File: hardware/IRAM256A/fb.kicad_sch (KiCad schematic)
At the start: 48 parts

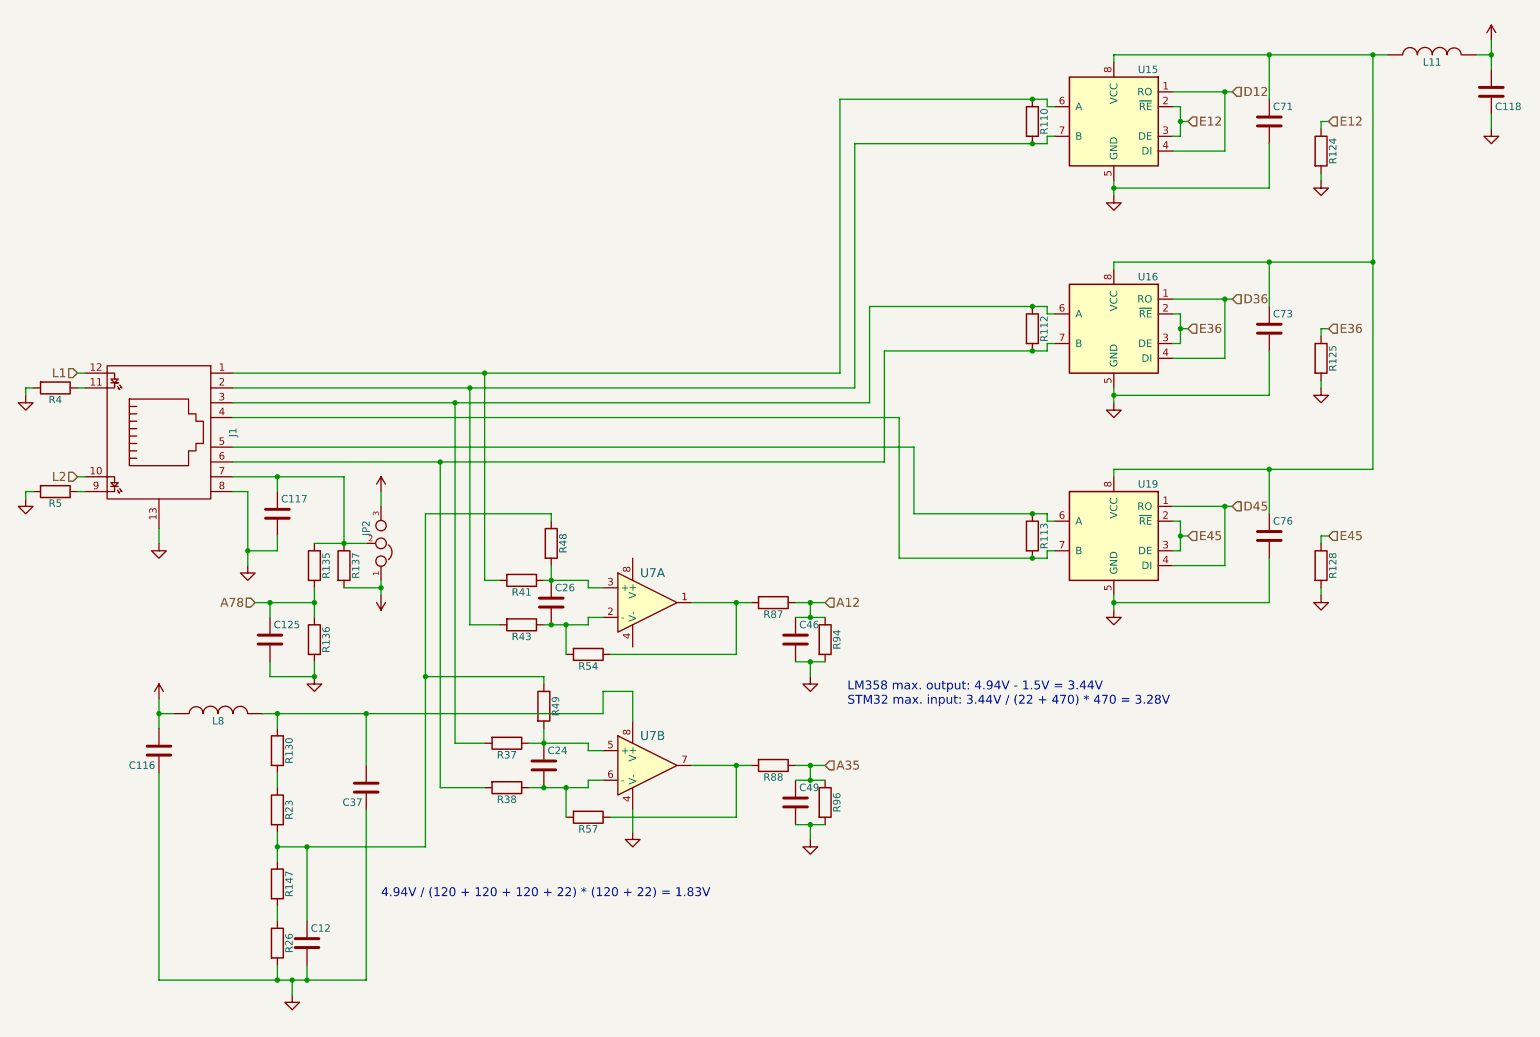
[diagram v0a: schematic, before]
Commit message: Structure change + kicad 3d models updated
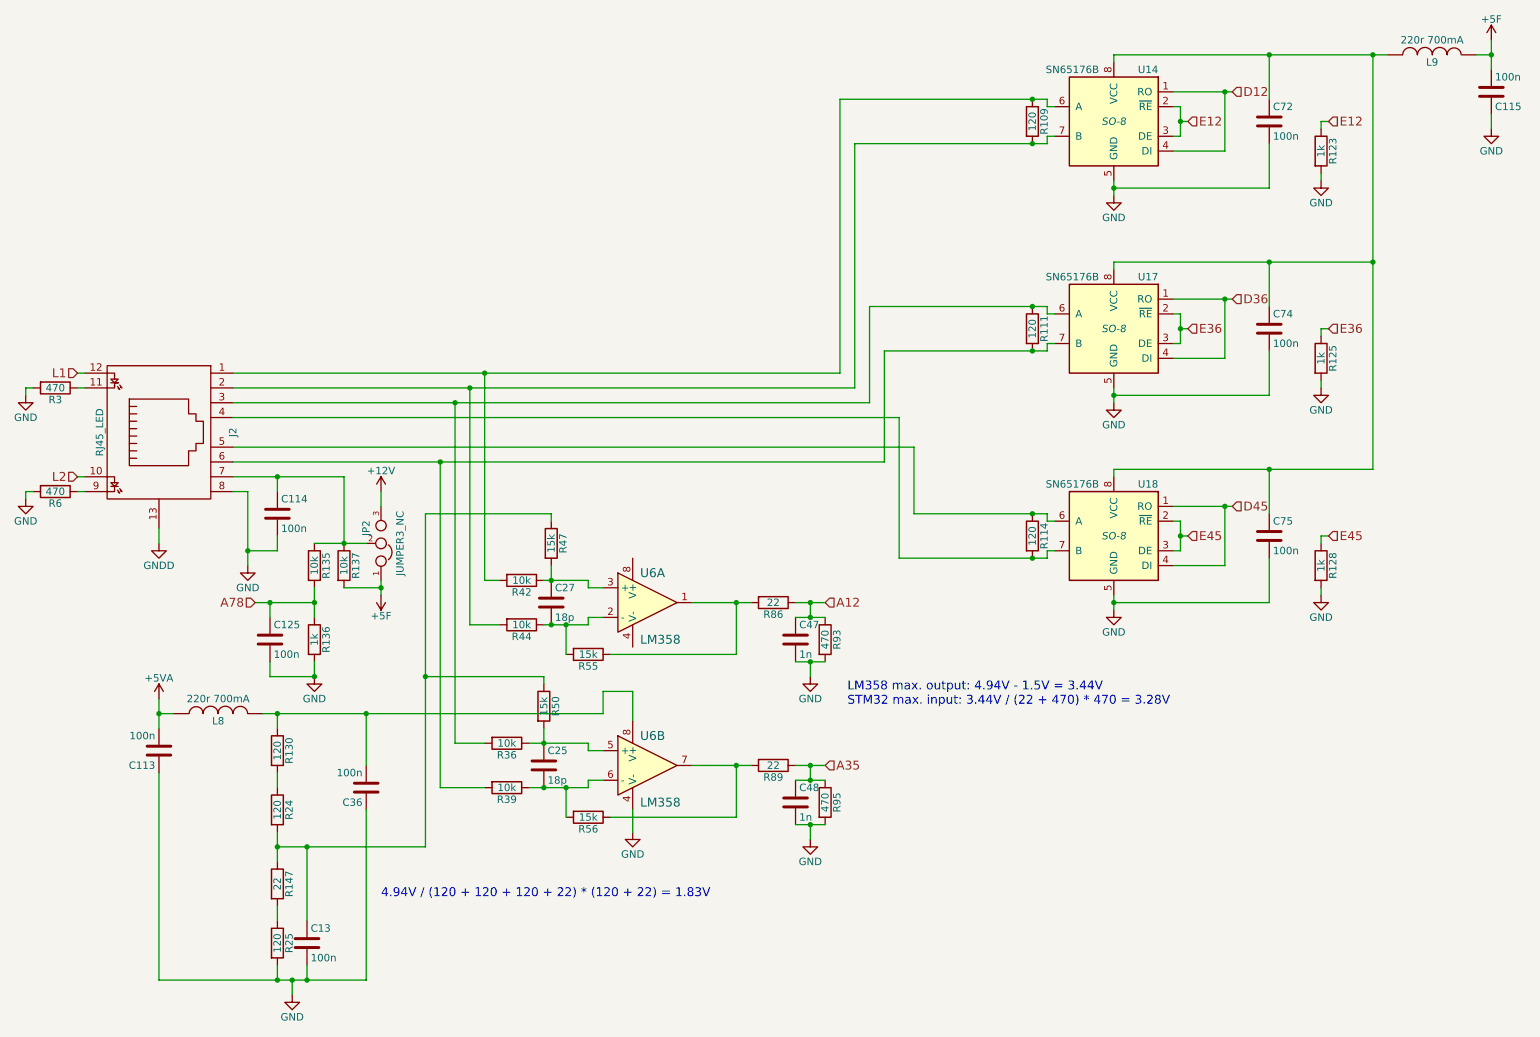
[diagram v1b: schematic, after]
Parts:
- C113: renamed from C116; value (none) -> 100n; footprint (none) -> stmbl:C_0603
- C114: renamed from C117; value (none) -> 100n; footprint (none) -> stmbl:C_0603
- C115: renamed from C118; value (none) -> 100n; footprint (none) -> stmbl:C_0603
- C125: value (none) -> 100n; footprint (none) -> stmbl:C_0603
- C13: renamed from C12; value (none) -> 100n; footprint (none) -> stmbl:C_0603
- C25: renamed from C24; value (none) -> 18p; footprint (none) -> stmbl:C_0603
- C27: renamed from C26; value (none) -> 18p; footprint (none) -> stmbl:C_0603
- C36: renamed from C37; value (none) -> 100n; footprint (none) -> stmbl:C_0603
- C47: renamed from C46; value (none) -> 1n; footprint (none) -> stmbl:C_0603
- C48: renamed from C49; value (none) -> 1n; footprint (none) -> stmbl:C_0603
- C72: renamed from C71; value (none) -> 100n; footprint (none) -> stmbl:C_0603
- C74: renamed from C73; value (none) -> 100n; footprint (none) -> stmbl:C_0603
- C75: renamed from C76; value (none) -> 100n; footprint (none) -> stmbl:C_0603
- J2: renamed from J1; value (none) -> RJ45_LED; footprint (none) -> stmbl:RJ45_LED
- JP2: value (none) -> JUMPER3_NC; footprint (none) -> stmbl:SOLDER_JUMPER_3_NC
- L8: value (none) -> 220r 700mA; footprint (none) -> stmbl:R_0603
- L9: renamed from L11; value (none) -> 220r 700mA; footprint (none) -> stmbl:R_0603
- R109: renamed from R110; value (none) -> 120; footprint (none) -> stmbl:R_0603
- R111: renamed from R112; value (none) -> 120; footprint (none) -> stmbl:R_0603
- R114: renamed from R113; value (none) -> 120; footprint (none) -> stmbl:R_0603
- R123: renamed from R124; value (none) -> 1k; footprint (none) -> stmbl:R_0603
- R125, R128, R136: value (none) -> 1k; footprint (none) -> stmbl:R_0603
- R130: value (none) -> 120; footprint (none) -> stmbl:R_0603
- R135, R137: value (none) -> 10k; footprint (none) -> stmbl:R_0603
- R147: value (none) -> 22; footprint (none) -> stmbl:R_0603
- R24: renamed from R23; value (none) -> 120; footprint (none) -> stmbl:R_0603
- R25: renamed from R26; value (none) -> 120; footprint (none) -> stmbl:R_0603
- R3: renamed from R4; value (none) -> 470; footprint (none) -> stmbl:R_0603
- R36: renamed from R37; value (none) -> 10k; footprint (none) -> stmbl:R_0603
- R39: renamed from R38; value (none) -> 10k; footprint (none) -> stmbl:R_0603
- R42: renamed from R41; value (none) -> 10k; footprint (none) -> stmbl:R_0603
- R44: renamed from R43; value (none) -> 10k; footprint (none) -> stmbl:R_0603
- R47: renamed from R48; value (none) -> 15k; footprint (none) -> stmbl:R_0603
- R50: renamed from R49; value (none) -> 15k; footprint (none) -> stmbl:R_0603
- R55: renamed from R54; value (none) -> 15k; footprint (none) -> stmbl:R_0603
- R56: renamed from R57; value (none) -> 15k; footprint (none) -> stmbl:R_0603
- R6: renamed from R5; value (none) -> 470; footprint (none) -> stmbl:R_0603
- R86: renamed from R87; value (none) -> 22; footprint (none) -> stmbl:R_0603
- R89: renamed from R88; value (none) -> 22; footprint (none) -> stmbl:R_0603
- R93: renamed from R94; value (none) -> 470; footprint (none) -> stmbl:R_0603
- R95: renamed from R96; value (none) -> 470; footprint (none) -> stmbl:R_0603
- U14: renamed from U15; value (none) -> SN65176B; footprint (none) -> SO-8
- U17: renamed from U16; value (none) -> SN65176B; footprint (none) -> SO-8
- U18: renamed from U19; value (none) -> SN65176B; footprint (none) -> SO-8
- U6: renamed from U7; value (none) -> LM358; footprint (none) -> stmbl:SOIC-8-N
